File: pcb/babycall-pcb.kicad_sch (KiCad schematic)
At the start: 13 parts, among them U1 ESP32-C3-MINI-1-H4X, U2 BQ24074RGTR

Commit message: Schematic almost done
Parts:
- added C7, C8, C9: 100nF, PCM_JLCPCB:C_0402, symbol PCM_JLCPCB-Capacitors:0402,100nF
- added D1: USBLC6-2SC6_C2827654, jlcpcb:SOT-23-6_L2.9-W1.6-P0.95-LS2.8-BL, symbol JLCPCB:USBLC6-2SC6_C2827654
- added R6: 10kΩ, PCM_JLCPCB:R_0402, symbol PCM_JLCPCB-Resistors:0402,10kΩ
- added SW1, SW2: TS-1187A-B-A-B, jlcpcb:SW-SMD_4P-L5.1-W5.1-P3.70-LS6.5-TL_H1.5, symbol JLCPCB:TS-1187A-B-A-B
- added U3: AP2112K-3.3, Package_TO_SOT_SMD:SOT-23-5, symbol Regulator_Linear:AP2112K-3.3
- added U4: ICS-43434_C5656610, jlcpcb:MIC-SMD_6P-L3.5-W2.7-P0.90-BL, symbol JLCPCB:ICS-43434_C5656610
- added USB1: TYPE-C 16PIN 2MD(073), jlcpcb:USB-C-SMD_TYPE-C-6PIN-2MD-073, symbol JLCPCB:TYPE-C16PIN2MD(073)
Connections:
- net +3V3: now also R6.1, U3.5 (VOUT), U4.5 (VDD)
- net +4.4V: now also U3.1 (VIN), U3.3 (EN)
- net +5V: now also D1.5 (VBUS), USB1.11 (VBUS), USB1.2 (VBUS)
- net GND: now also C7.2, C8.2, C9.2, D1.2 (GND), SW1.3 (C), SW2.3 (C), U3.2 (GND), U4.3 (GND), USB1.1 (GND), USB1.12 (GND)
- net EN: now reaches C3.1, R1.2, U1.8 (EN)
- net EN: now also C9.1, SW2.1 (A)
- net MEMS_WS: now reaches U1.20 (IO6)
- net MEMS_WS: now also U4.1 (WS)
- net MEMS_LR: now reaches U1.21 (IO7)
- net MEMS_LR: now also U4.2 (LR)
- net MEMS_SD: now reaches U1.22 (IO8)
- net MEMS_SD: now also U4.6 (SD)
- net MEMS_SCK: now reaches U1.23 (IO9)
- net MEMS_SCK: now also R6.2, SW1.1 (A), U4.4 (SCK)
- net D+: now reaches U1.26 (IO18)
- net D+: now also D1.1 (IO1)
- net D-: now reaches U1.27 (IO19)
- net D-: now also D1.3 (IO2)
- new net: C7.1, USB1.13 (SHELL)
- new net: C8.1, USB1.14 (SHELL)
- new net DN: D1.4 (IO2), USB1.5 (DN2), USB1.7 (DN1)
- new net DP: D1.6 (IO1), USB1.6 (DP1), USB1.8 (DP2)
- no-connect marks 2 -> 29
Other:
- note added: "5.1K Resistors to GND When I get the symbol"
- note added: "Decoupling"
- note added: "Decoupling?"
- note added: "Verify pin semantics"
- note added: "Verify pins"

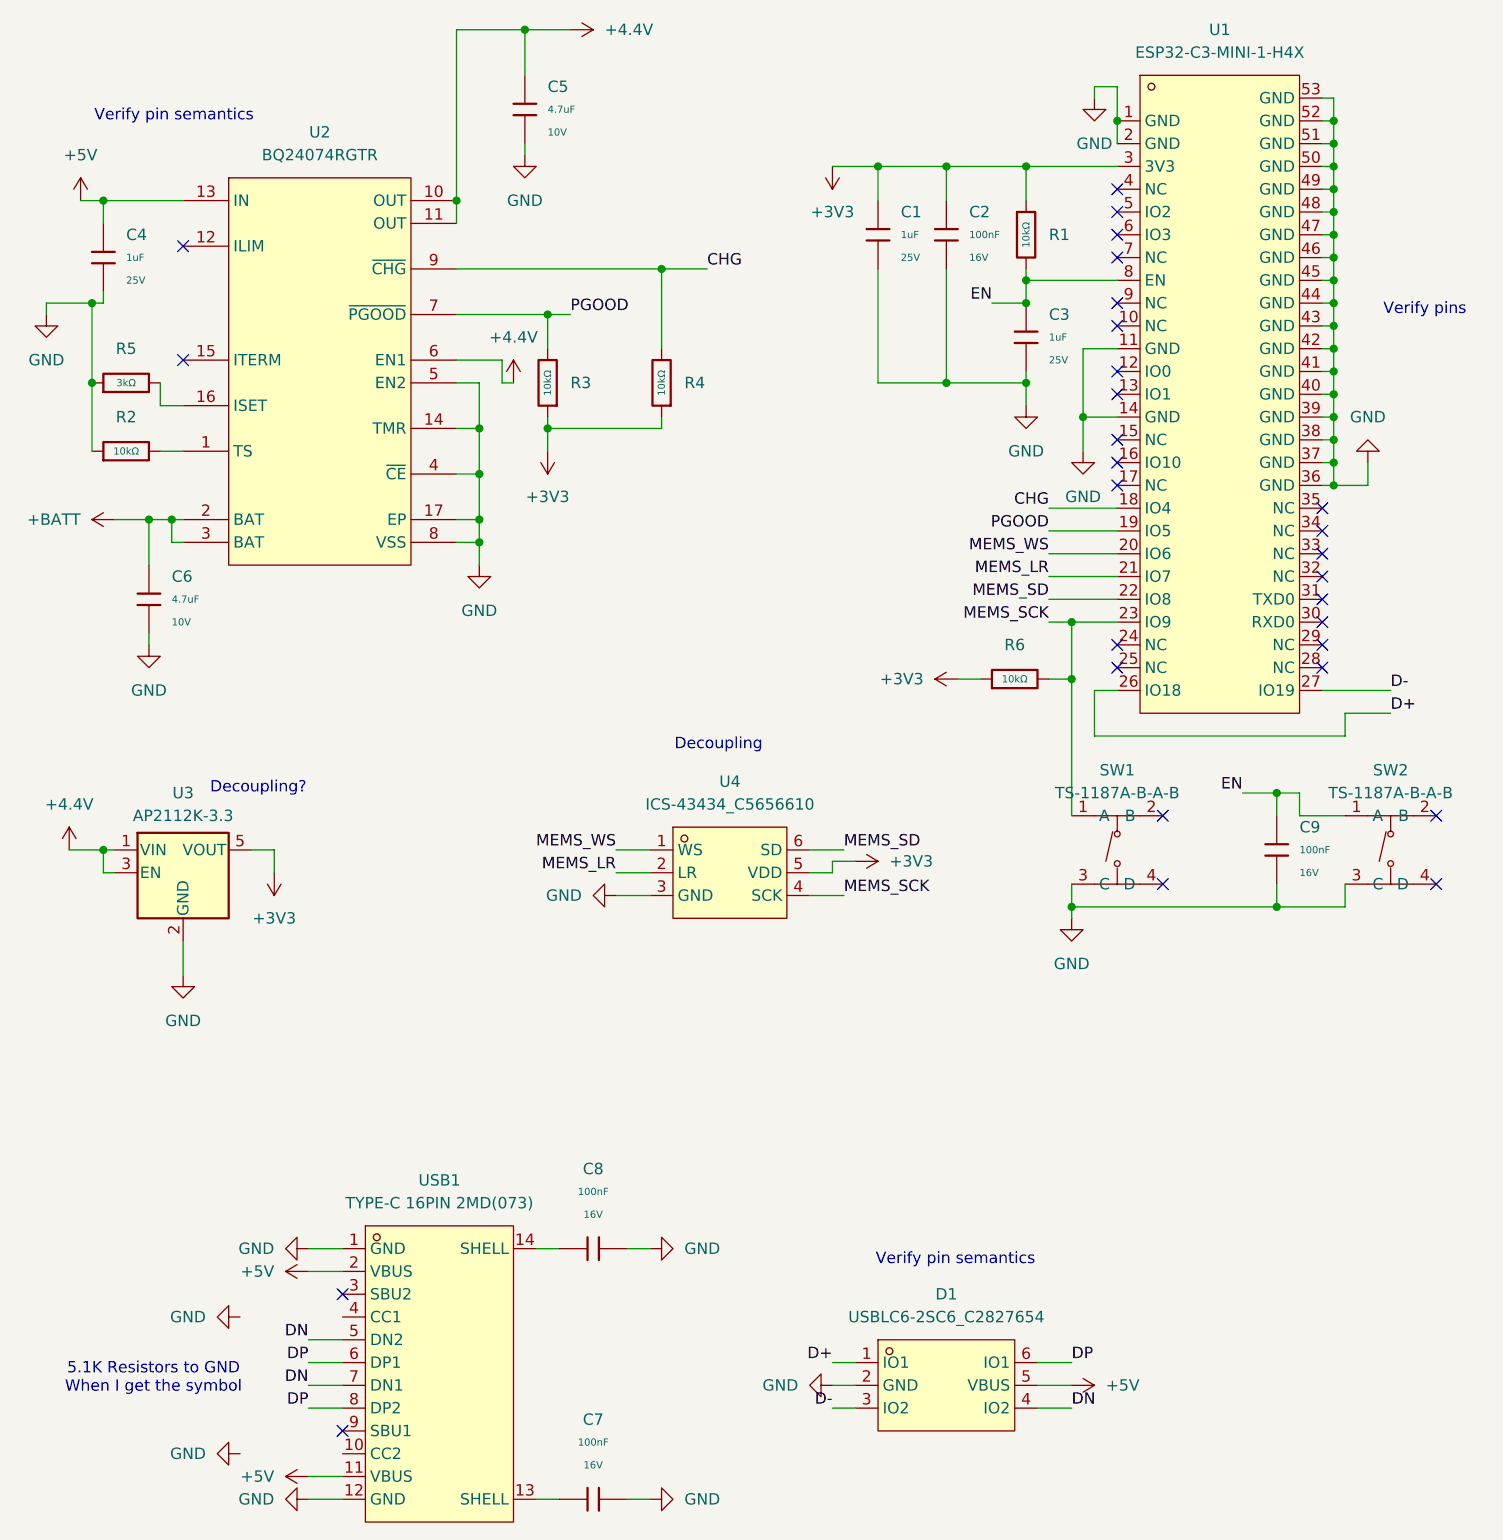
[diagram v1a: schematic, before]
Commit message: Added usb cc resistors
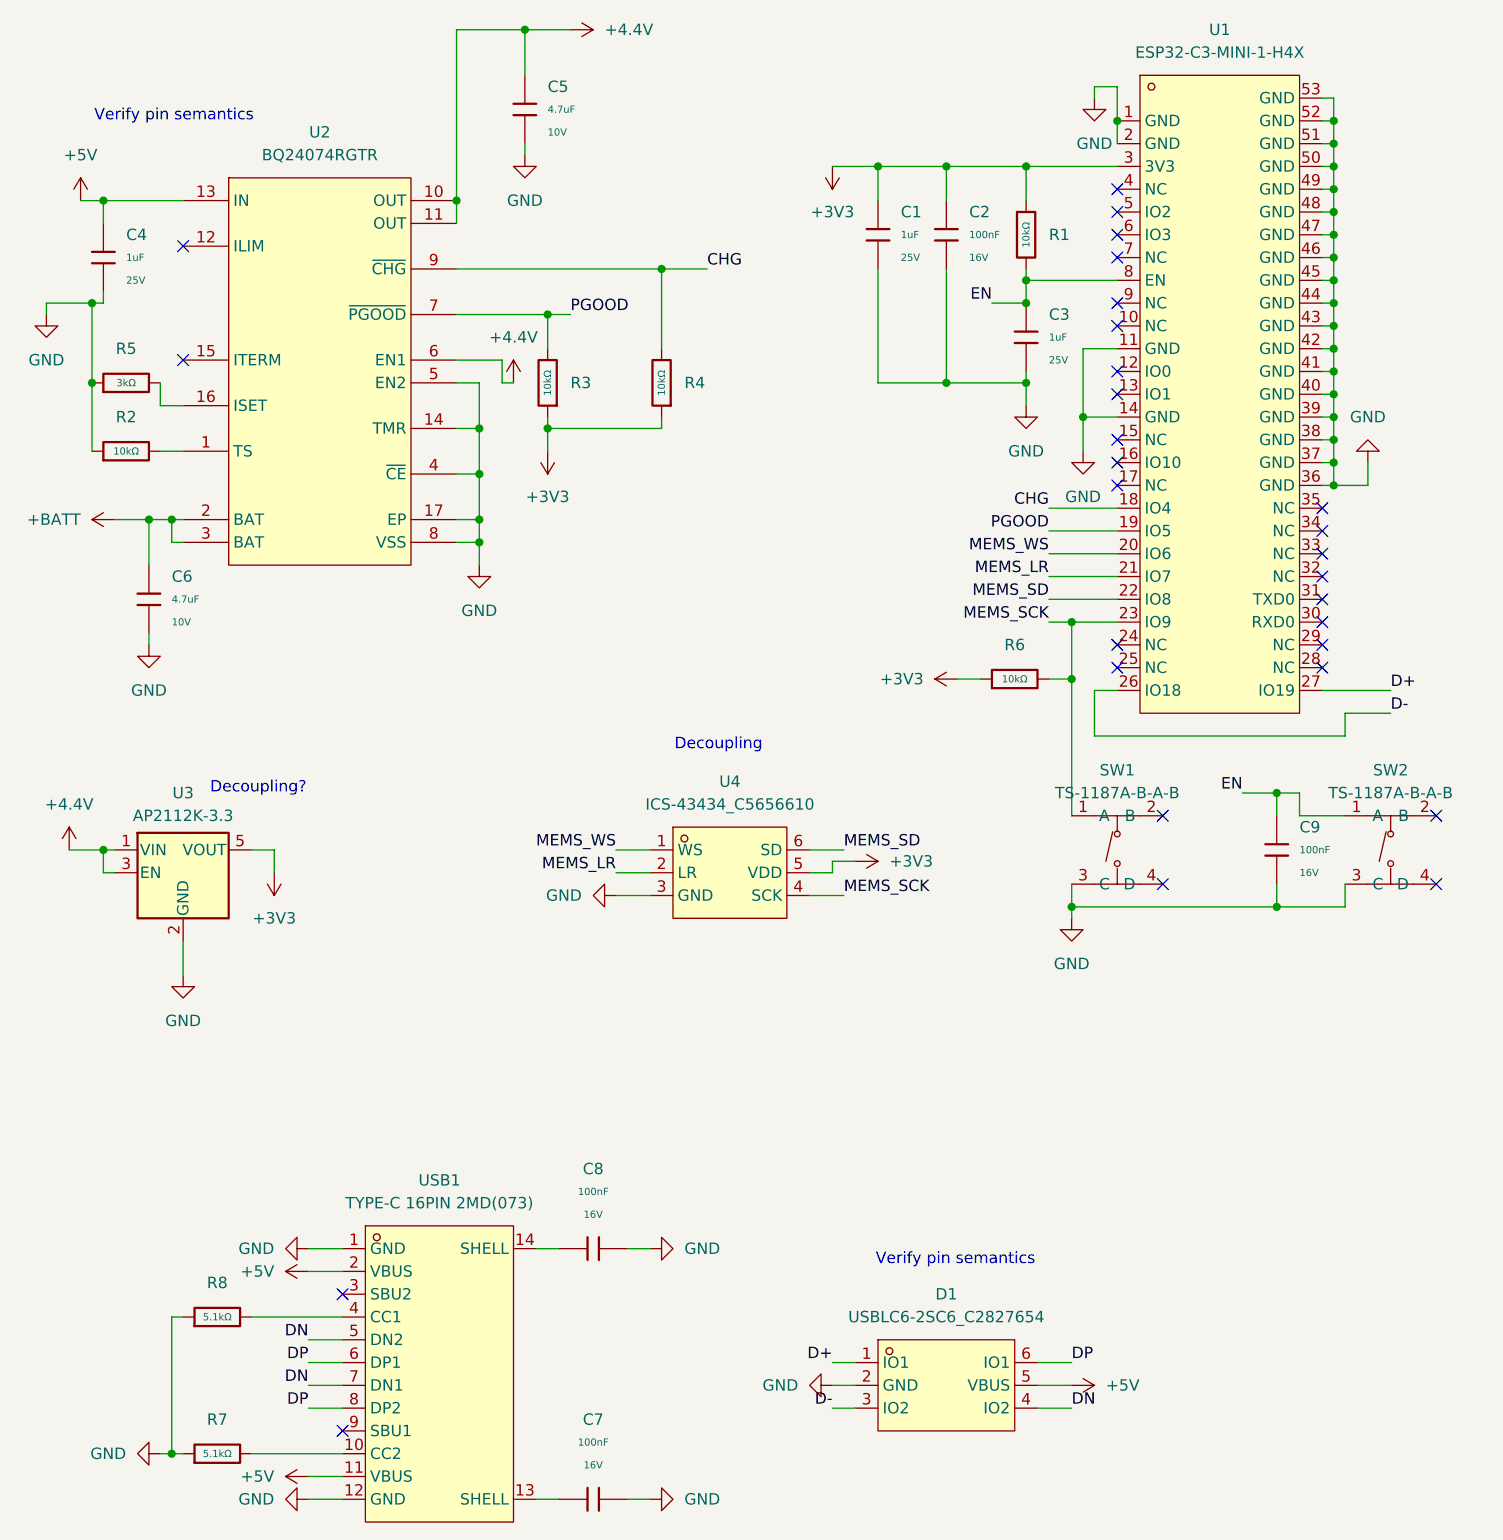
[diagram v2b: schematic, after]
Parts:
- added R7, R8: 5.1kΩ, PCM_JLCPCB:R_0402, symbol PCM_JLCPCB-Resistors:0402,5.1kΩ
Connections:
- net D+: now also U1.27 (IO19); no longer U1.26 (IO18)
- net D-: now also U1.26 (IO18); no longer U1.27 (IO19)
- net GND: now also R7.1, R8.1
- net at USB1.10 (CC2): now also R7.2
- net at USB1.4 (CC1): now also R8.2
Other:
- note removed: "5.1K Resistors to GND When I get the symbol"
- note removed: "Verify pins"
